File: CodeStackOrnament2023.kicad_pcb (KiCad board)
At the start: 2 copper layers, 70 x 70 mm, 35 parts, among them SW1 SW_SPST, U1 TLC555xD, U2 74VHC4040FT

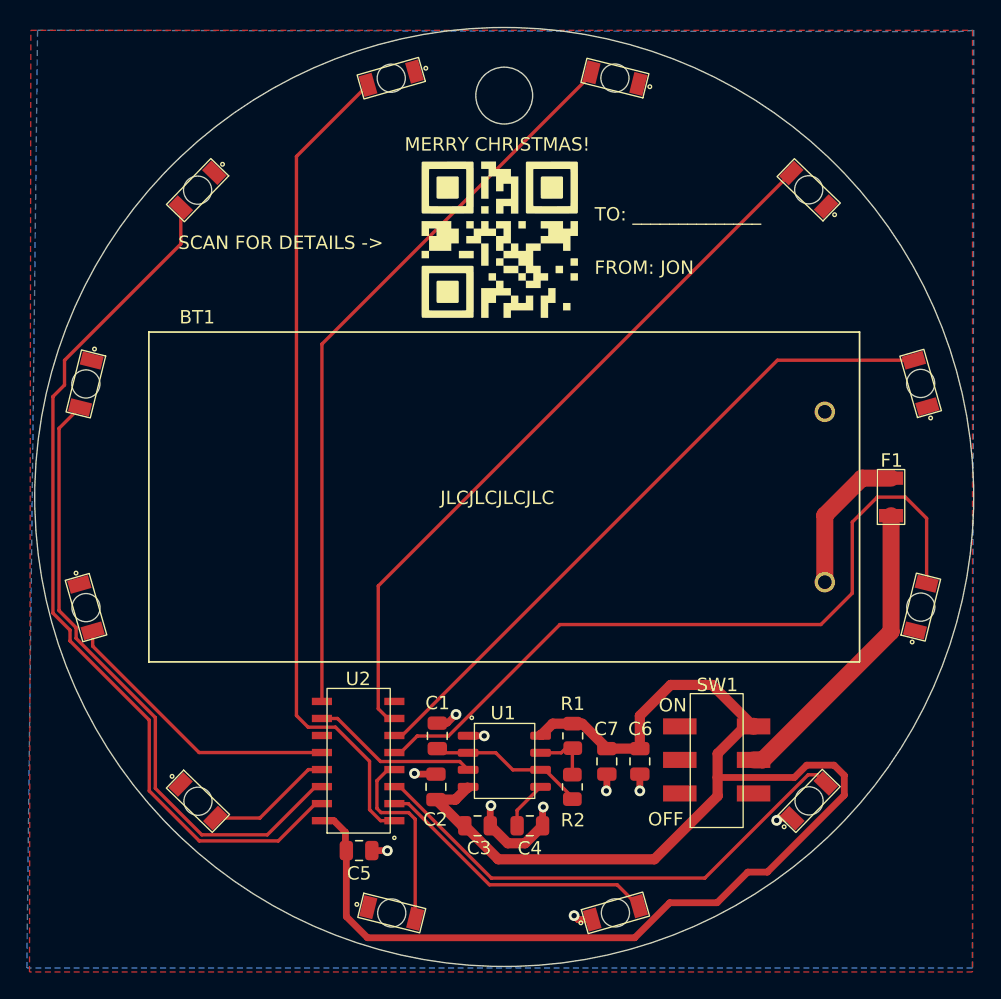
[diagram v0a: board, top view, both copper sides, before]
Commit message: finshed routing rev 1.b with reset circuit
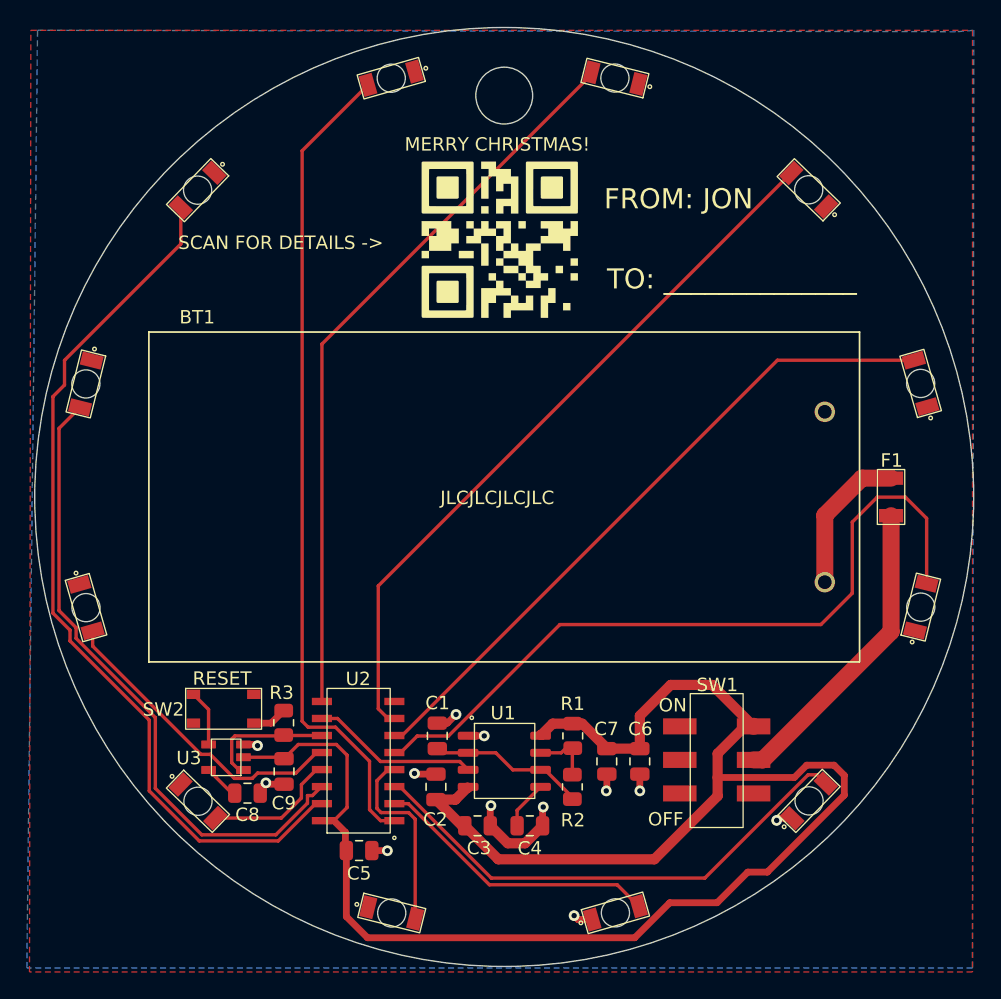
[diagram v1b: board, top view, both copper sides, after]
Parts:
- added C8: 0.1u, Capacitor_SMD:C_0805_2012Metric, F.Cu at (130.9, 126.8)
- added C9: 0.1u, Capacitor_SMD:C_0805_2012Metric, F.Cu at (133.7, 125.2)
- added R3: DNP, Resistor_SMD:R_0805_2012Metric, F.Cu at (133.7, 121.5)
- added SW2: RESET, CodeStackOrnament2023Footprints:PTS815_SWITCH, F.Cu at (126.9, 119.4)
- added U3: TPS3840PH, CodeStackOrnament2023Footprints:TPS3840_RESET, F.Cu at (130.7, 125.1)
- C3: value 1uF -> 10uF
- R1, R2: value 8k -> 12k
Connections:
- net Net-(U1-Q) renamed /CLK
- U2 pad 11: GND -> /RESET
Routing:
- net +3V0: track 118.2 -> 132.0 mm
- net /RESET: track 0.00 -> 9.73 mm
- net GND: track 19.3 -> 25.6 mm, vias 10 -> 12
- net Net-(U3-~{MR}): track 0.00 -> 4.21 mm
- net Net-(U3-CT): track 0.00 -> 2.67 mm
- net Net-(D9-A): track 21.5 -> 23.1 mm
- net Net-(D8-A): track 9.44 -> 10.0 mm
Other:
- board text added: "RESET"

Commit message: rev 1.b added a reset circuit to ensure counter starts at 0. Reorganizing schematic.
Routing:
- net GND: track 25.6 -> 26.1 mm
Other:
- board text added: "REV 1.B"
